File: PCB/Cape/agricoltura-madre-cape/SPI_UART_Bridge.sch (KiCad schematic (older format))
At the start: 1 part

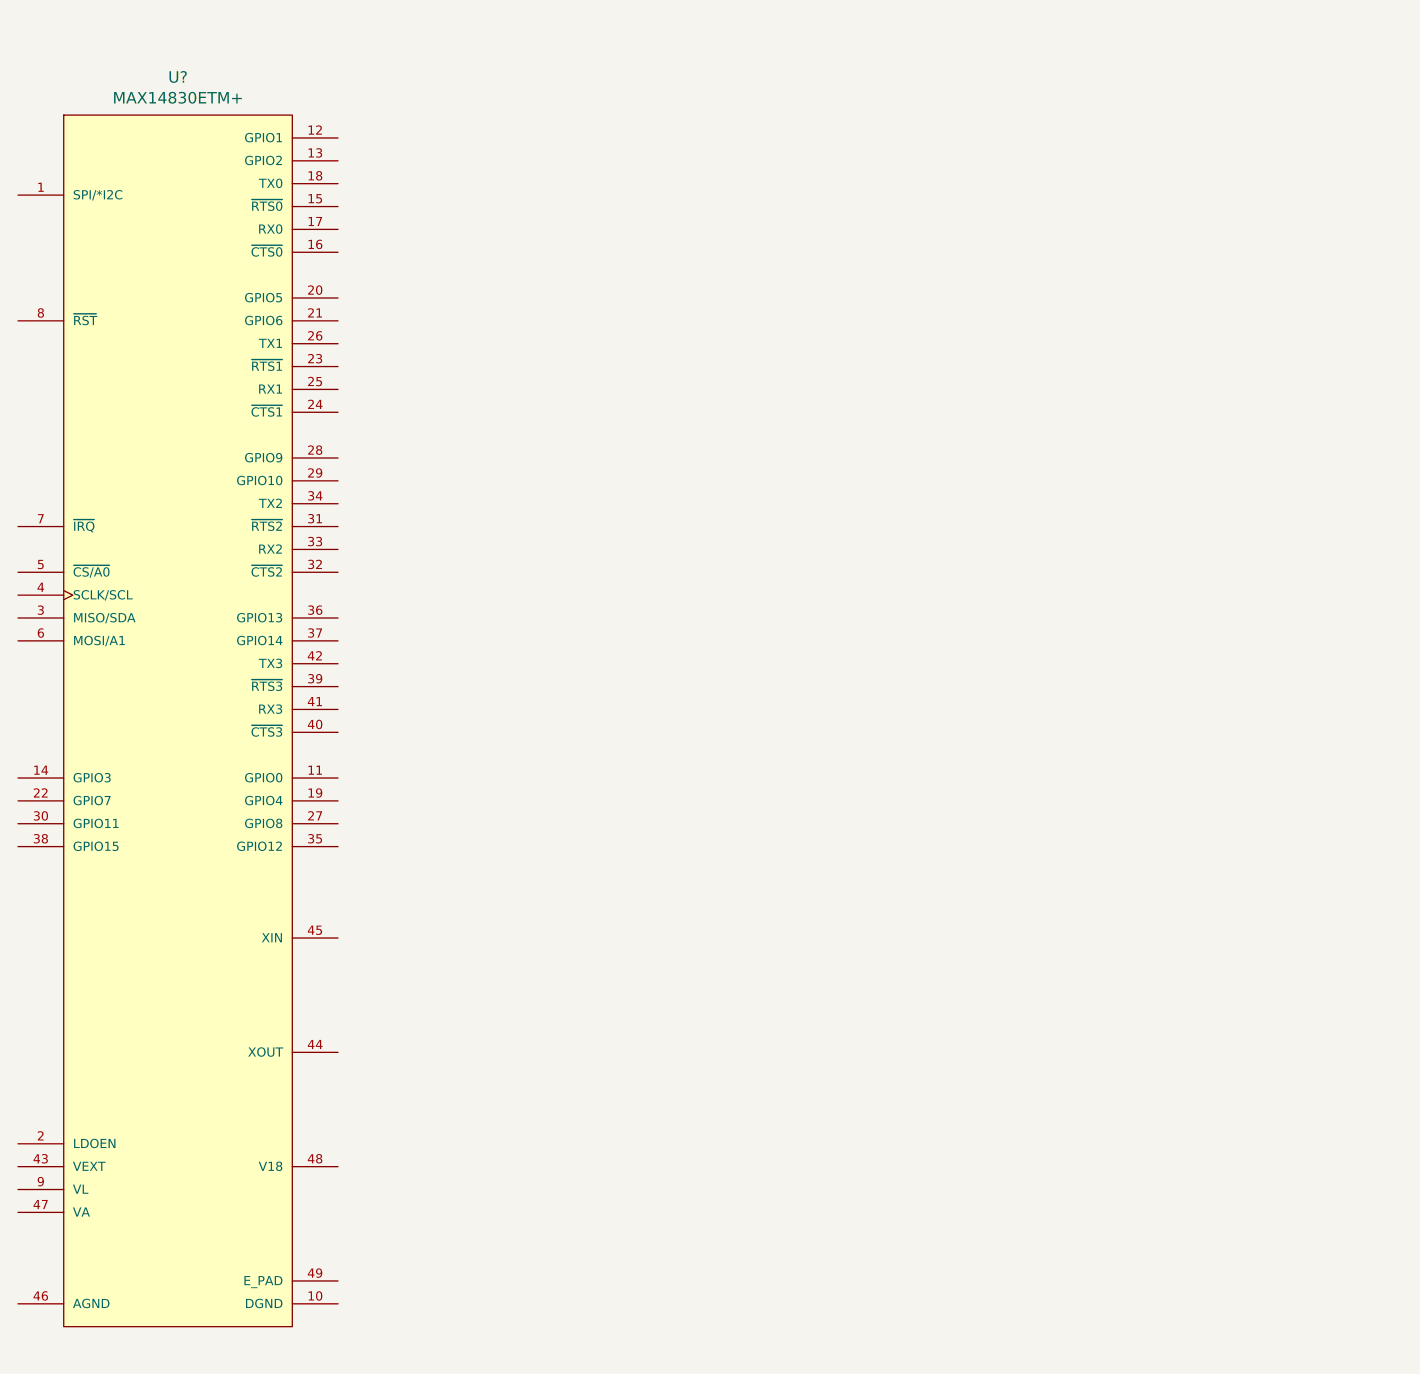
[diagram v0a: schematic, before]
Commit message: SPI UART Bridge
Fleshed out schematic for SPI UART bridge chip, realized we may not need it, now going to fork project and develop two versions in this same repository.
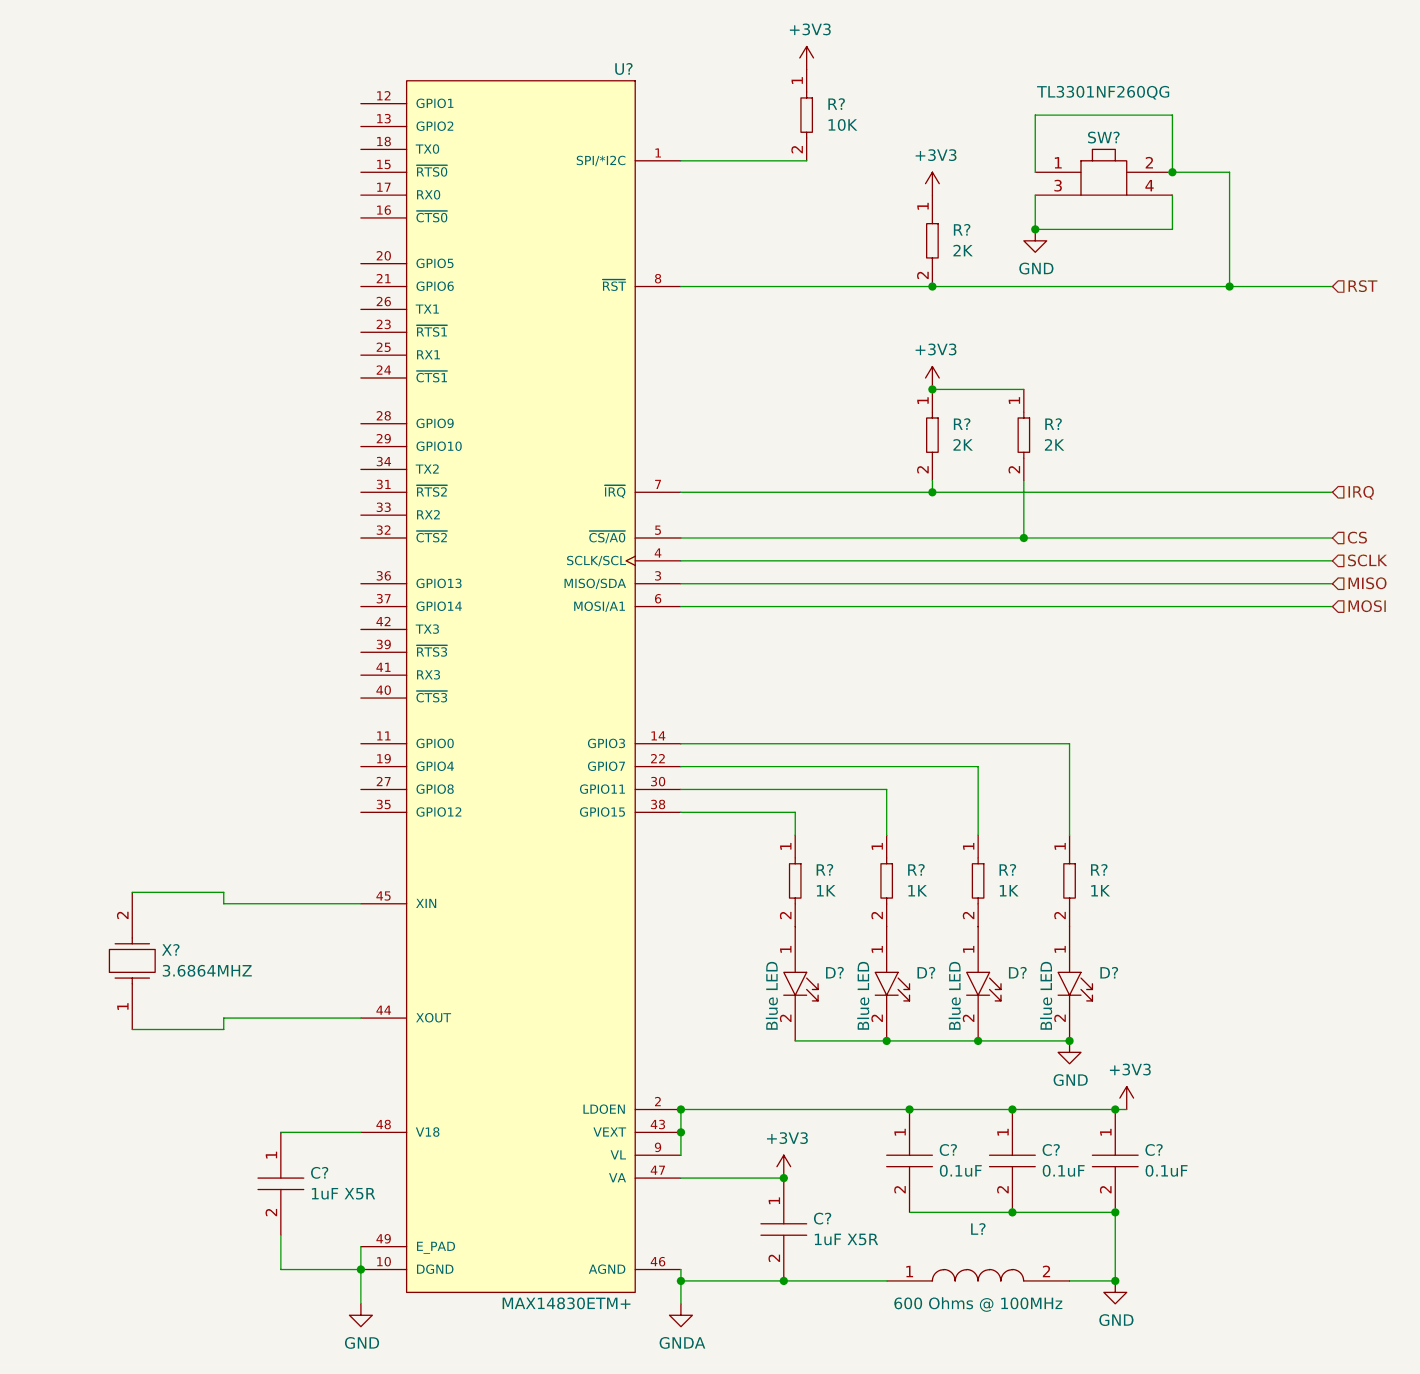
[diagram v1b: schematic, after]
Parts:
- added C? (x2): CC0603KRX5R7BB105, AVR-KiCAD-Lib-Capacitors:C0603, symbol AVR-KiCAD-Lib-Capacitors:CC0603KRX5R7BB105
- added C? (x3): C0402C104K9PACTU, AVR-KiCAD-Lib-Resistors:R0402, symbol AVR-KiCAD-Lib-Capacitors:C0402C104K9PACTU
- added D? (x4): LTST-C194TBKT, AVR-KiCAD-Lib-Diodes:LED0603, symbol AVR-KiCAD-Lib-Diodes:LTST-C194TBKT
- added L?: BLM15HG601SN1D, AVR-KiCAD-Lib-Inductors:BLM15HG601SN1D, symbol AVR-KiCAD-Lib-Inductors:BLM15HG601SN1D
- added R?: RC0402FR-0710KL, AVR-KiCAD-Lib-Resistors:R0402, symbol AVR-KiCAD-Lib-Resistors:RC0402FR-0710KL
- added R? (x3): RC0402FR-072KL, AVR-KiCAD-Lib-Resistors:R0402, symbol AVR-KiCAD-Lib-Resistors:RC0402FR-072KL
- added R? (x4): RC0402FR-071KL, AVR-KiCAD-Lib-Resistors:R0402, symbol AVR-KiCAD-Lib-Resistors:RC0402FR-071KL
- added SW?: TL3301NF260QG, AVR-KiCAD-Lib-Mech-Switches:TL3301NF260QG, symbol AVR-KiCAD-Lib-Mech-Switches:TL3301NF260QG
- added X?: ABLS-3.6864MHZ-B4-T, AVR-KiCAD-Lib-Oscillators:ABLS-3.6864MHZ-B4-T, symbol AVR-KiCAD-Lib-Oscillators-Clocks:ABLS-3.6864MHZ-B4-T
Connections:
- net at U?.1 (SPI/*I2C): now also R?.2
- net GND: now reaches U?.10 (DGND)
- net GND: now also U?.49 (E_PAD), C?.2, C?.2, C?.2, C?.2, D?.2, D?.2, D?.2, D?.2, L?.2, SW?.3, SW?.4
- net at U?.14 (GPIO3): now also R?.1
- net +3V3: now reaches U?.2 (LDOEN)
- net +3V3: now also U?.43 (VEXT), U?.47 (VA), U?.9 (VL), C?.1, C?.1, C?.1, C?.1, R?.1, R?.1, R?.1, R?.1
- net at U?.22 (GPIO7): now also R?.1
- net MISO: now reaches U?.3 (MISO/SDA)
- net at U?.30 (GPIO11): now also R?.1
- net at U?.38 (GPIO15): now also R?.1
- net SCLK: now reaches U?.4 (SCLK/SCL)
- net at U?.44 (XOUT): now also X?.1
- net at U?.45 (XIN): now also X?.2
- net GNDA: now reaches U?.46 (AGND)
- net GNDA: now also C?.2, L?.1
- net at U?.48 (V18): now also C?.1
- net CS: now reaches U?.5 (~CS/A0~)
- net CS: now also R?.2
- net MOSI: now reaches U?.6 (MOSI/A1)
- net IRQ: now reaches U?.7 (~IRQ~)
- net IRQ: now also R?.2
- net RST: now reaches U?.8 (~RST~)
- net RST: now also R?.2, SW?.1, SW?.2
- new net: D?.1, R?.2 (x4)
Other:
- moved on the sheet: U?
